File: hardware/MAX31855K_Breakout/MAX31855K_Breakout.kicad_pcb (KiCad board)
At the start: 2 copper layers, 35 x 35 mm, 16 parts, among them J1 Conn_01x02_Socket, J2 Conn_01x02_Socket, J3 Conn_01x03_Socket, U1 MAX31855KASA, U2 TPS631000

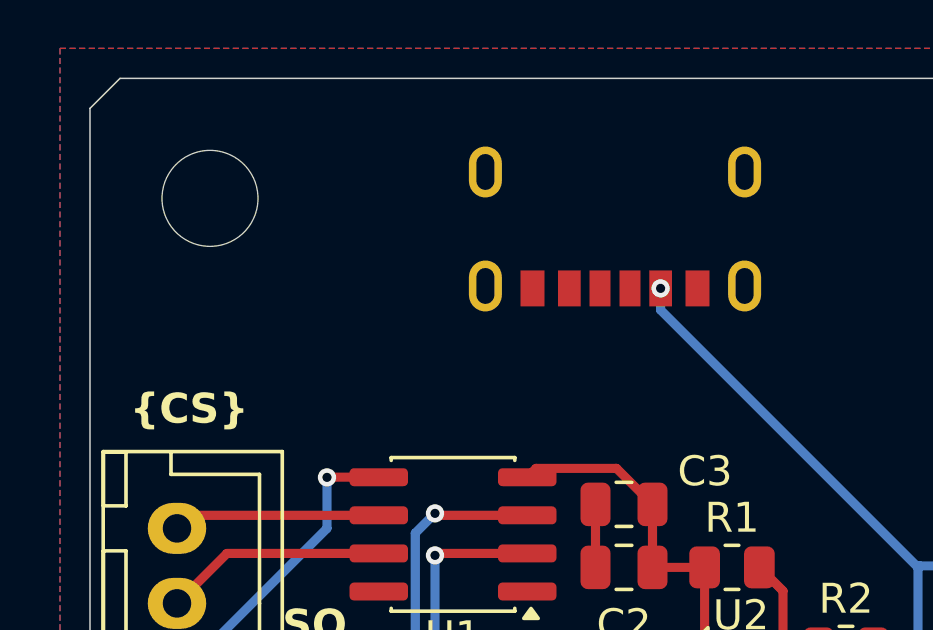
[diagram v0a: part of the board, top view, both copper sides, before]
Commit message: fix: add 5.1k resistors to USB-C CC pins (#5)
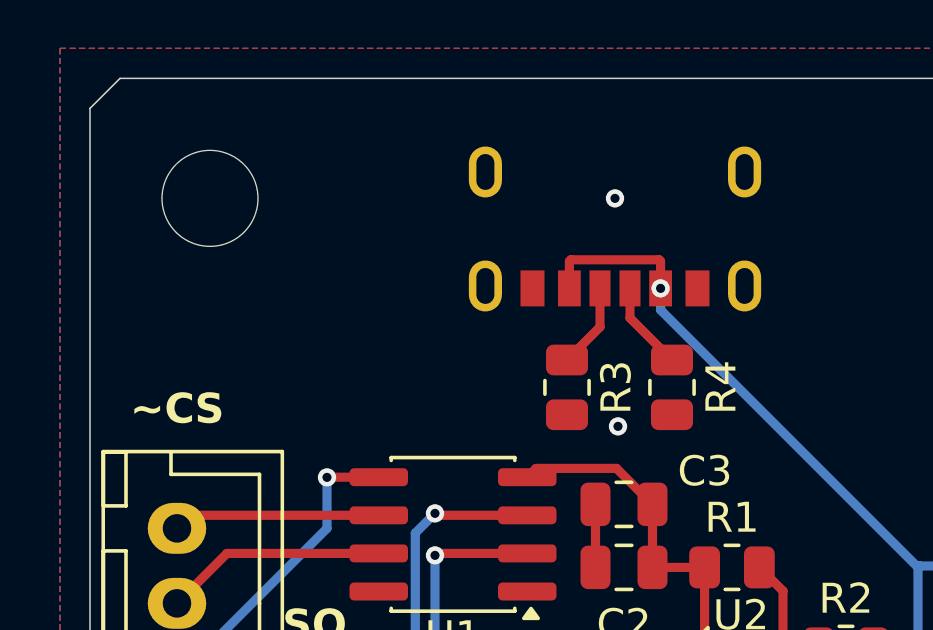
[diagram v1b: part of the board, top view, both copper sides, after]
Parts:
- added R3: 5.1k, Resistor_SMD:R_0805_2012Metric, F.Cu at (141.9, 105.3)
- added R4: 5.1k, Resistor_SMD:R_0805_2012Metric, F.Cu at (145.4, 105.3)
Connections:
- USB_C1 pad A12: unconnected-(USB_C1-GND-PadA12) -> GND
- USB_C1 pad A5: unconnected-(USB_C1-CC1-PadA5) -> Net-(USB_C1-CC1)
- USB_C1 pad A9: unconnected-(USB_C1-VBUS-PadA9) -> Net-(J2-Pin_1)
- USB_C1 pad B5: unconnected-(USB_C1-CC2-PadB5) -> Net-(USB_C1-CC2)
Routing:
- net Net-(J2-Pin_1): track 34.5 -> 39.4 mm
- net Net-(USB_C1-CC1): track 0.00 -> 2.97 mm
- net Net-(USB_C1-CC2): track 0.00 -> 2.84 mm
- net GND: vias 1 -> 3
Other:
- board text added: "~CS"
- board text removed: "{CS}"

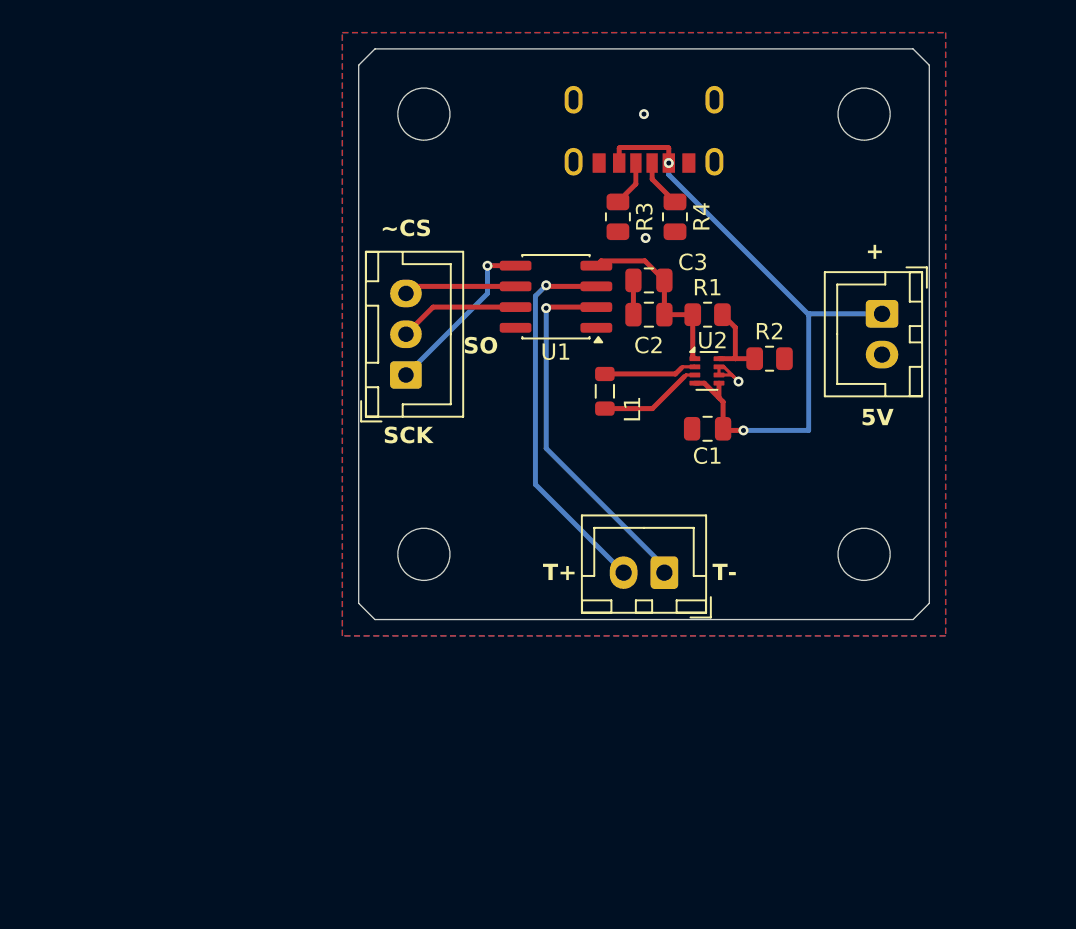
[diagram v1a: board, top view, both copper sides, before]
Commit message: feat: add mosfet to board for signal (#8)
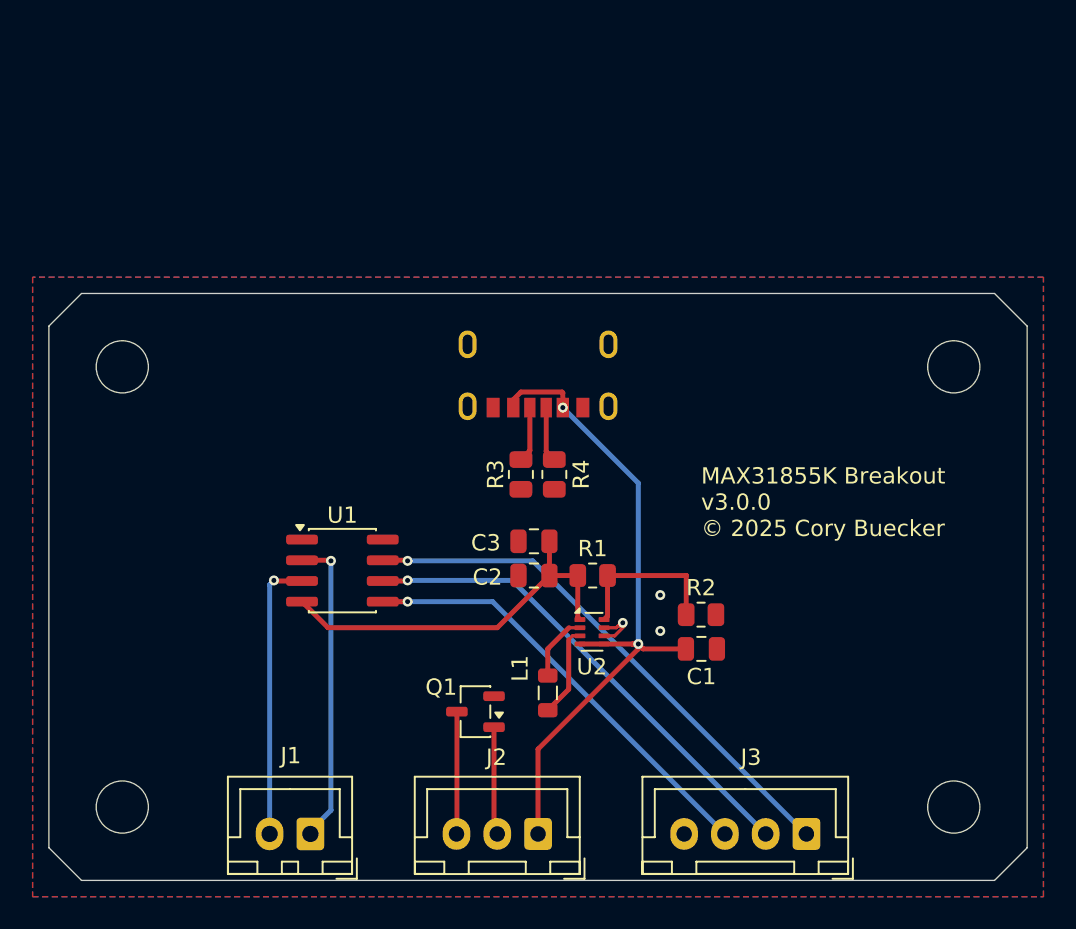
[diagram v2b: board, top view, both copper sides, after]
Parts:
- added Q1: Q_NMOS_GSD, Package_TO_SOT_SMD:SOT-23-3, F.Cu at (133.2, 135.7)
- J2: value Conn_01x02_Socket -> Conn_01x03_Socket; footprint Connector_JST:JST_XH_B2B-XH-A_1x02_P2.50mm_Vertical -> Connector_JST:JST_XH_B3B-XH-A_1x03_P2.50mm_Vertical
- J3: value Conn_01x03_Socket -> Conn_01x04_Socket; footprint Connector_JST:JST_XH_B3B-XH-A_1x03_P2.50mm_Vertical -> Connector_JST:JST_XH_B4B-XH-A_1x04_P2.50mm_Vertical
- moved H1 48.1 mm to (111.5, 114.5)
- moved H2 48.1 mm to (111.5, 141.5)
- moved J2 38.2 mm to (137.0, 143.2), turned to 180 degrees
- moved J3 37.4 mm to (153.5, 143.2), turned to 180 degrees
- moved H3 36.0 mm to (162.5, 114.5)
- moved H4 36.0 mm to (162.5, 141.5)
- moved J1 27.0 mm to (123.0, 143.2)
- moved U1 21.3 mm to (125.0, 127.0), turned to 0 degrees
- moved L1 18.8 mm to (137.6, 134.5)
- moved C2 17.5 mm to (136.8, 127.3)
- moved C3 17.5 mm to (136.8, 125.2)
- moved R1 17.5 mm to (140.3, 127.3)
- moved U2 17.5 mm to (140.3, 130.8)
- moved R4 17.4 mm to (138.0, 121.1)
- moved R3 16.9 mm to (135.9, 121.1)
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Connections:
- J2 pad 2: GND -> Net-(J2-Signal)
- J3 pad 1: Net-(J3-Pin_1) -> Net-(J3-SO)
- J3 pad 2: Net-(J3-Pin_2) -> Net-(J3-~{CS})
- J3 pad 3: Net-(J3-Pin_3) -> Net-(J3-SCK)
- U1 pad 5: Net-(J3-Pin_1) -> Net-(J3-SCK)
- U1 pad 6: Net-(J3-Pin_3) -> Net-(J3-~{CS})
- U1 pad 7: Net-(J3-Pin_2) -> Net-(J3-SO)
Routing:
- net Net-(J3-SO): track 0.00 -> 32.9 mm, vias 0 -> 1
- net Net-(J3-~{CS}): track 0.00 -> 30.1 mm, vias 0 -> 1
- net Net-(J3-SCK): track 0.00 -> 27.0 mm, vias 0 -> 1
- net Net-(U1-V_{CC}): track 11.4 -> 23.8 mm
- net Net-(J3-Pin_1): track 10.5 -> 0.00 mm, vias 1 -> 0
- net Net-(J2-GND): track 0.00 -> 7.51 mm
- net Net-(J3-Pin_2): track 7.41 -> 0.00 mm
- net Net-(J3-Pin_3): track 6.91 -> 0.00 mm
- net Net-(J2-Signal): track 0.00 -> 6.63 mm
- net Net-(J1-T+): track 23.2 -> 17.4 mm
- net Net-(U2-FB): track 5.22 -> 10.0 mm
- net Net-(J1-T-): track 22.3 -> 19.1 mm
- net GND: track 5.54 -> 3.01 mm
- net Net-(J2-+5V): track 39.4 -> 41.9 mm
- net Net-(U2-LX2): track 5.96 -> 4.15 mm
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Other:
- board size 35 x 35 mm -> 60 x 36 mm
- board text added: "MAX31855K Breakout v3.0.0 © 2025 Cory Buecker"
- board text removed: "+"
- board text removed: "5V"
- board text removed: "SCK"
- board text removed: "SO"
- board text removed: "T+"
- board text removed: "T-"
- board text removed: "~CS"

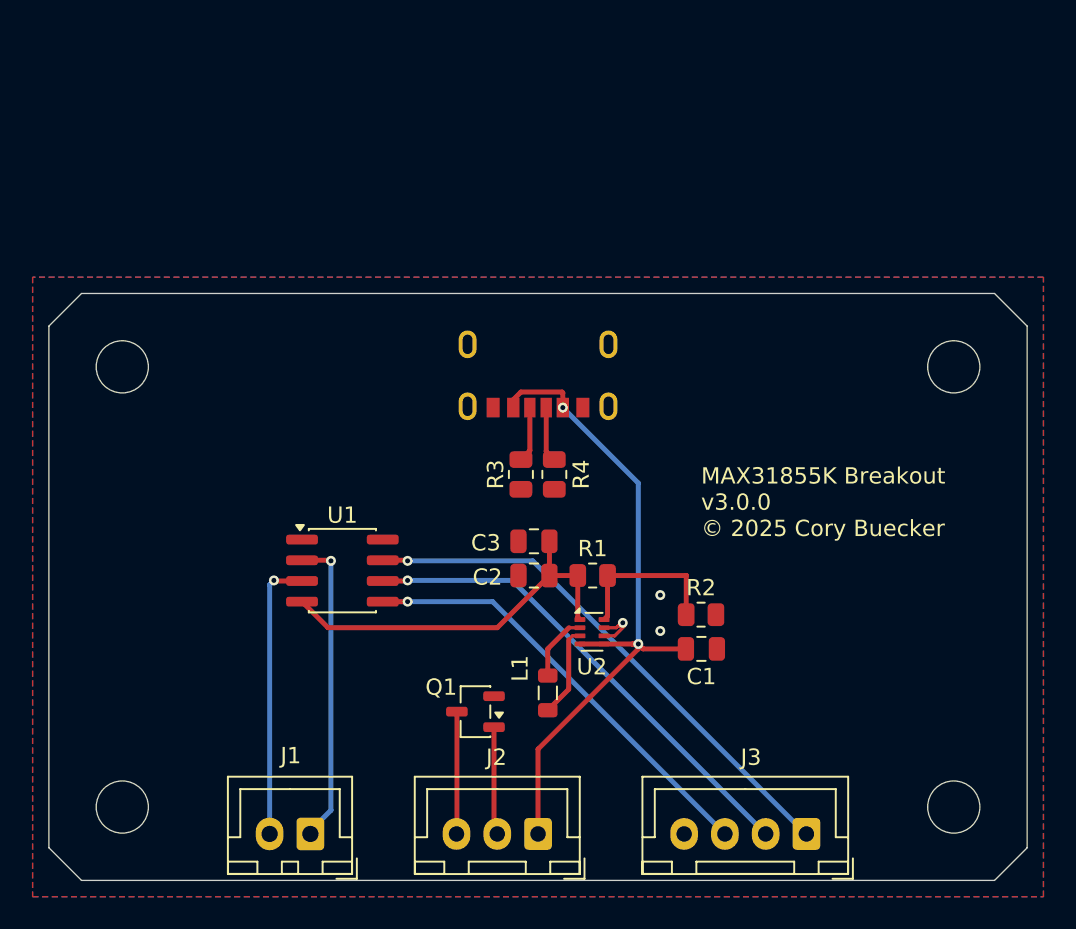
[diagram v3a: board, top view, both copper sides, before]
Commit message: chore: add copy of temp. sensor with reorganized pins (#11)
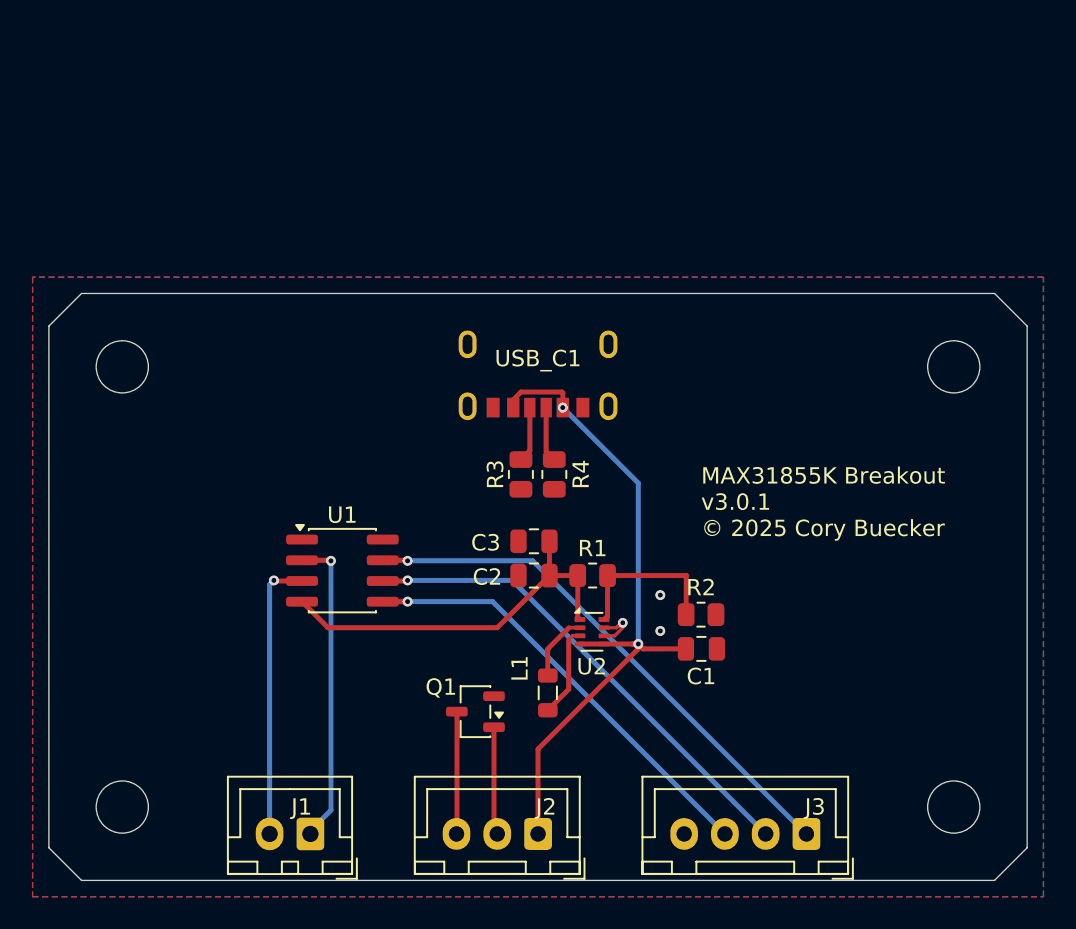
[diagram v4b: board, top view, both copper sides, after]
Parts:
- J1: value Conn_01x02_Socket -> Temperature Probe Connector
- J2: value Conn_01x03_Socket -> SSR Connector
- J3: value Conn_01x04_Socket -> SPI Connector
- USB_C1: footprint User:USB_C_Receptacle -> Reflow_Oven:USB_C_Receptacle
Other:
- board text added: "MAX31855K Breakout ${REVISION} © 2025 Cory Buecker"
- board text removed: "MAX31855K Breakout v3.0.0 © 2025 Cory Buecker"

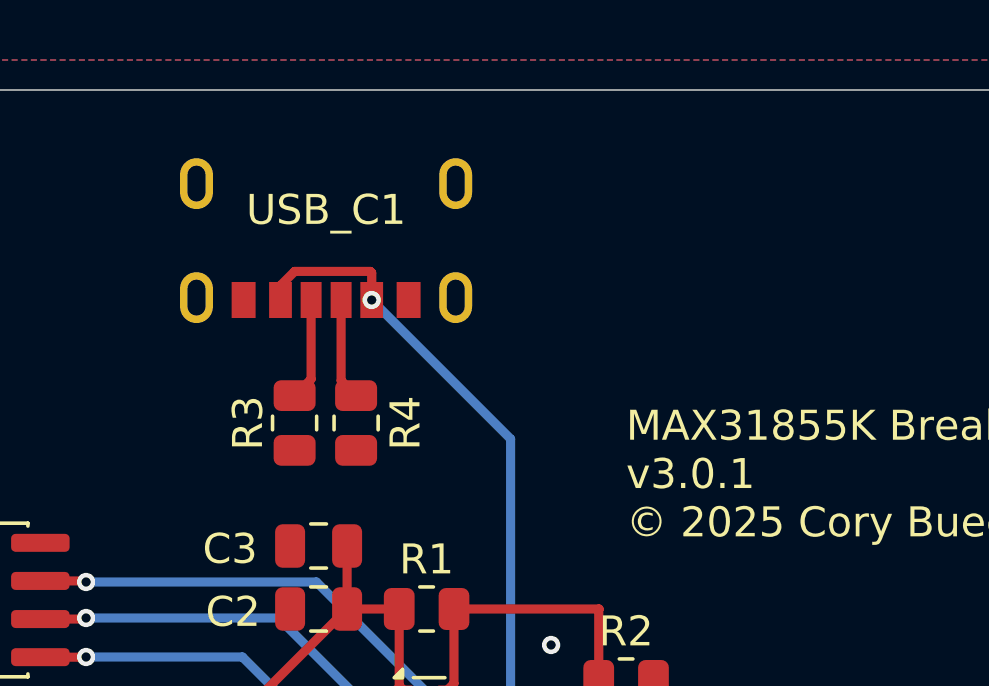
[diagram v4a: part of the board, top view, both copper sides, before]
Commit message: chore: lint hardware (#12)
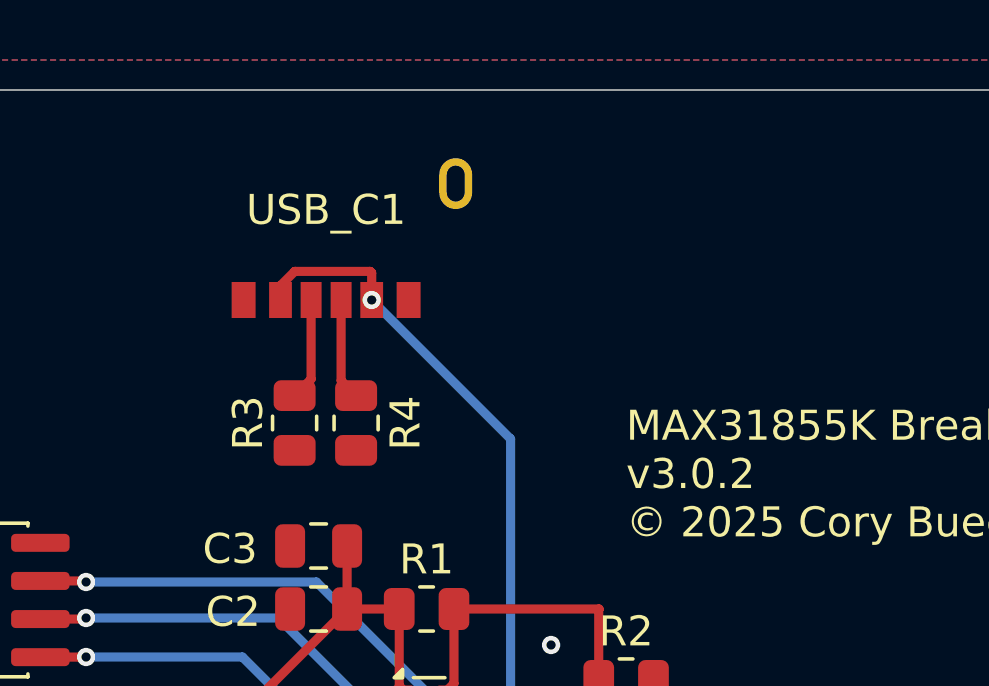
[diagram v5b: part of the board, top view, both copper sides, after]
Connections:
- USB_C1 pad S1: (no net) -> GND
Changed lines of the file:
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@@
 	(title_block
 		(title "MAX31855K Breakout")
-		(date "2025-11-29")
-		(rev "v3.0.1")
+		(date "2025-12-01")
+		(rev "v3.0.2")
 		(company "Cory Buecker")
 		(comment 1 "© 2025 Stanton Cory Buecker")
@@
 			)
 		)
-		(property "Datasheet" "~"
+		(property "Datasheet" "https://www.onsemi.com/download/data-sheet/pdf/nds7002a-d.pdf"
 			(at 0 0 0)
 			(layer "F.Fab")
@@
 	)
 	(footprint "Reflow_Oven:USB_C_Receptacle"
-		(locked yes)
 		(layer "F.Cu")
 		(at 137 114)
@@
 		(sheetname "/")
 		(sheetfile "MAX31855K_Breakout.kicad_sch")
-		(attr smd)
+		(attr through_hole)
 		(fp_rect
 			(start -5 -4)
@@
 			)
 		)
+		(pad "" np_thru_hole oval
+			(at -4.32 -0.88 180)
+			(size 1.1 1.7)
+			(drill oval 0.6 1.2)
+			(layers "*.Cu" "*.Mask")
+		)
+		(pad "" np_thru_hole oval
+			(at -4.32 2.92 180)
+			(size 1.1 1.7)
+			(drill oval 0.6 1.2)
+			(layers "*.Cu" "*.Mask")
+		)
+		(pad "" np_thru_hole oval
+			(at 4.32 2.92 180)
+			(size 1.1 1.7)
+			(drill oval 0.6 1.2)
+			(layers "*.Cu" "*.Mask")
+		)
 		(pad "A5" smd rect
 			(at 0.5 3 180)
@@
 			(pinfunction "GND")
 			(pintype "power_out")
-		)
-		(pad "S1" thru_hole oval
-			(at -4.32 -0.88 180)
-			(size 1.1 1.7)
-			(drill oval 0.6 1.2)
-			(property pad_prop_heatsink)
-			(layers "*.Cu" "*.Mask")
-			(remove_unused_layers no)
-		)
-		(pad "S1" thru_hole oval
-			(at -4.32 2.92 180)
-			(size 1.1 1.7)
-			(drill oval 0.6 1.2)
-			(property pad_prop_heatsink)
-			(layers "*.Cu" "*.Mask")
-			(remove_unused_layers no)
 		)
 		(pad "S1" thru_hole oval
@@
 			(size 1.1 1.7)
 			(drill oval 0.6 1.2)
-			(property pad_prop_heatsink)
 			(layers "*.Cu" "*.Mask")
 			(remove_unused_layers no)
-		)
-		(pad "S1" thru_hole oval
-			(at 4.32 2.92 180)
-			(size 1.1 1.7)
-			(drill oval 0.6 1.2)
-			(property pad_prop_heatsink)
-			(layers "*.Cu" "*.Mask")
-			(remove_unused_layers no)
+			(net 1 "GND")
+			(pinfunction "Shield")
+			(pintype "power_in")
 		)
 		(embedded_fonts no)
@@
 					(thickness 0.15)
 				)
-			)
-		)
-		(property "DigiKey Part Number" "296-TPS631000DRLRCT-ND"
-			(at 0 0 0)
-			(unlocked yes)
-			(layer "F.Fab")
-			(hide yes)
-			(effects
-				(font
-					(size 1 1)
-					(thickness 0.15)
-				)
